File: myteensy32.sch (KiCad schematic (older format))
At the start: 31 parts, among them J1 Conn_01x14_Male, J2 Conn_01x14_Male, J3 USB_C_Receptacle_USB2.0, SW1 RESET, SW2 PROG, U1 MKL04Z32VLC4, U2 MK20DX256VLH7, U3 MCP2562-E-SN, U4 NJM2884U1, Y2 16MHz

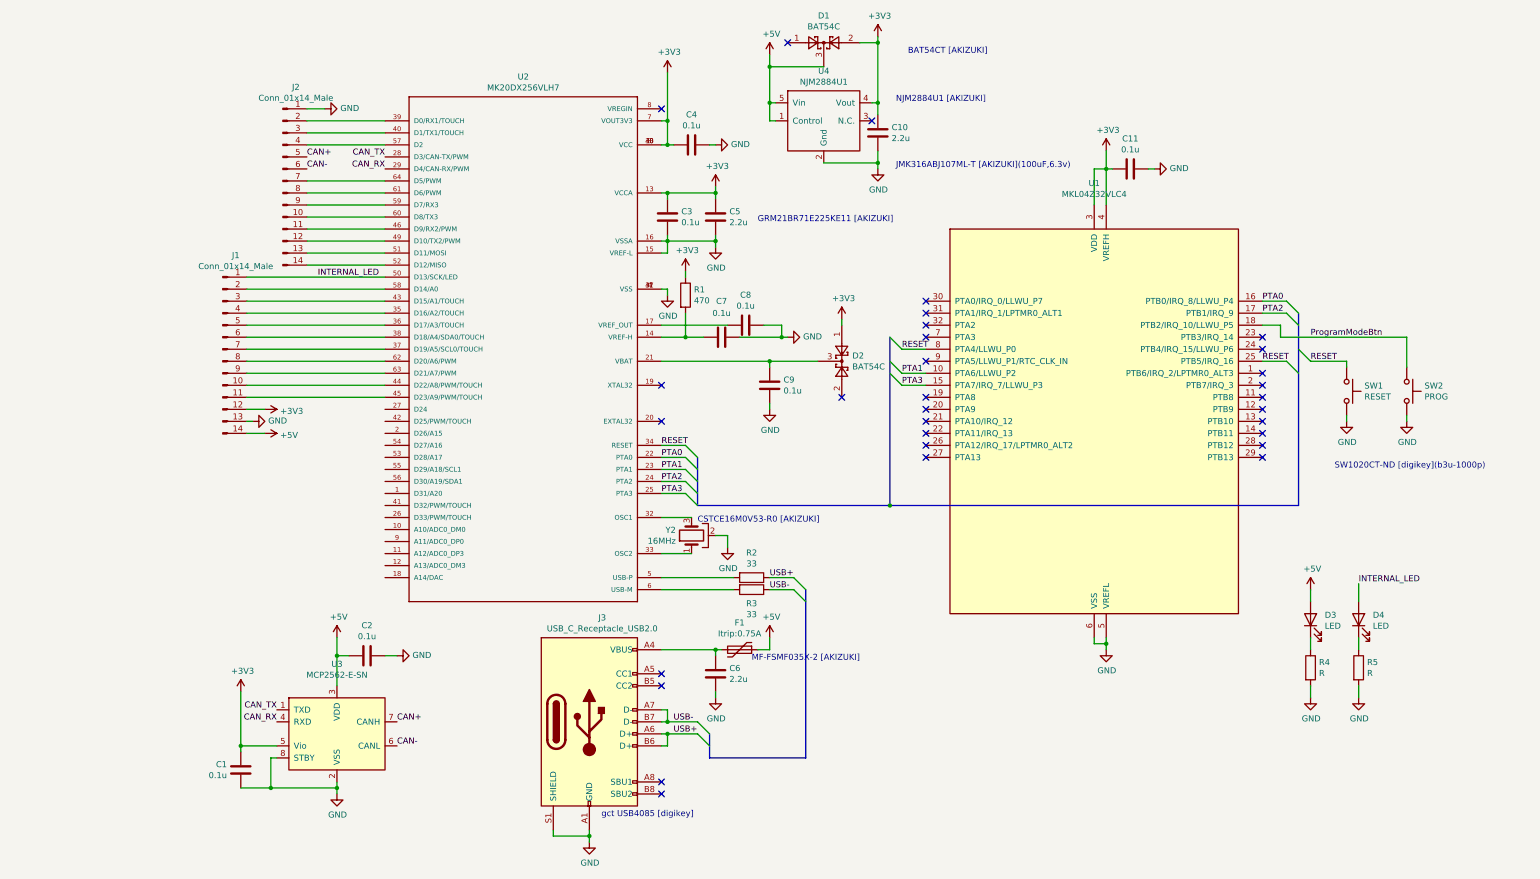
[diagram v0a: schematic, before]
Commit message: Connectorを追加
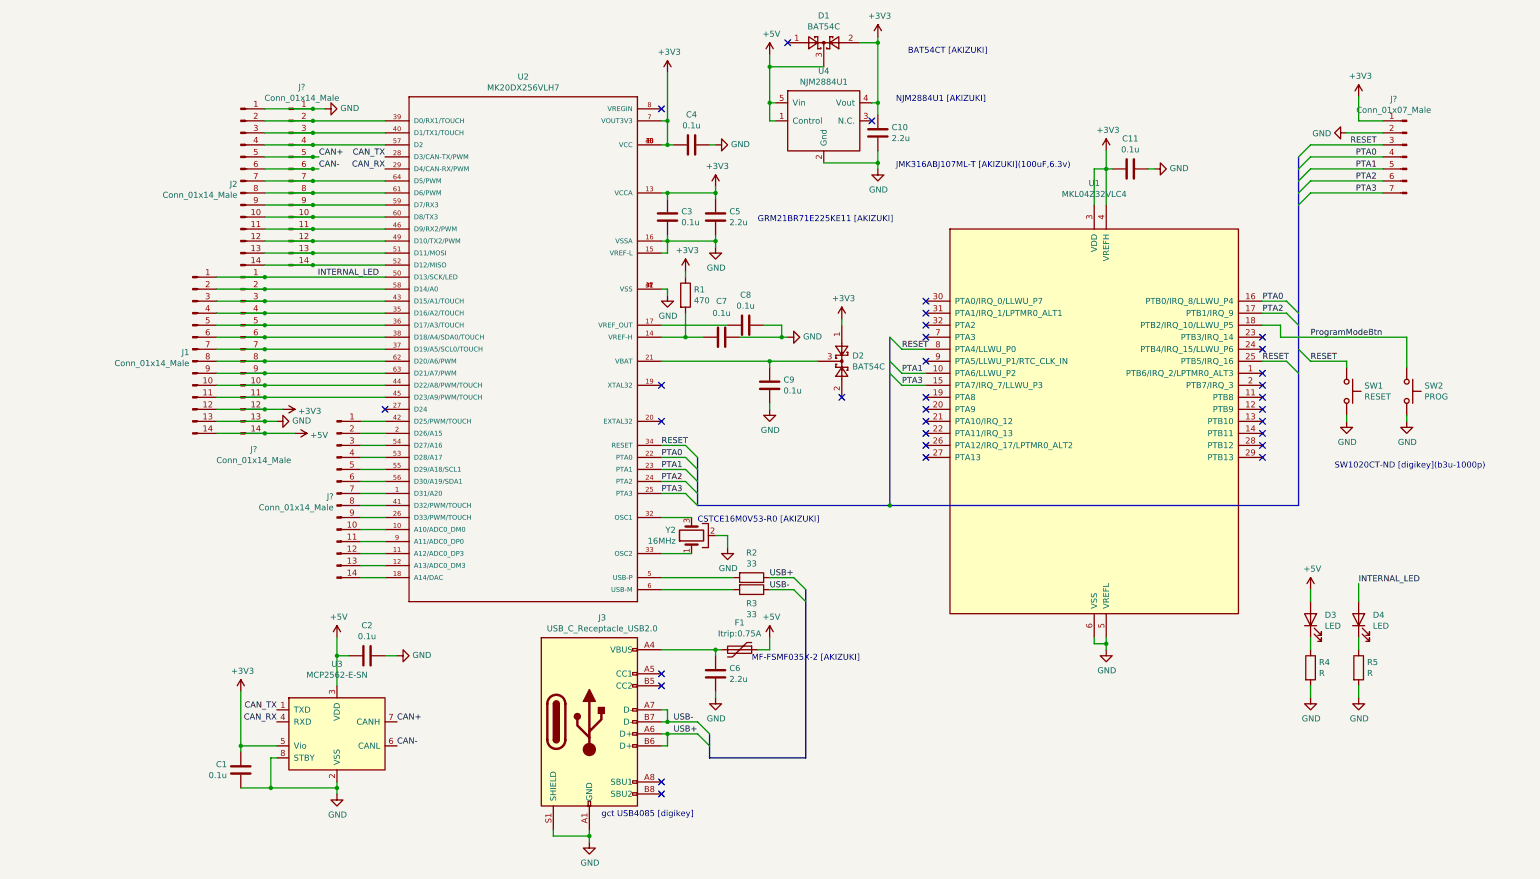
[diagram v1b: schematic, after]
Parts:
- added J?: Conn_01x07_Male, symbol Connector:Conn_01x07_Male
- added J? (x3): Conn_01x14_Male, Connector_PinHeader_2.54mm:PinHeader_1x14_P2.54mm_Vertical, symbol Connector:Conn_01x14_Male
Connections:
- net +3V3: now also J?.1 (Pin_1), J?.12 (Pin_12)
- net +5V: now also J?.14 (Pin_14)
- net CAN+: now also J?.5 (Pin_5)
- net CAN-: now also J?.6 (Pin_6)
- net GND: now also J?.1 (Pin_1), J?.13 (Pin_13), J?.2 (Pin_2)
- net INTERNAL_LED: now also J?.1 (Pin_1)
- net PTA0: now also J?.4 (Pin_4)
- net PTA1: now also J?.5 (Pin_5)
- net PTA2: now also J?.6 (Pin_6)
- net PTA3: now also J?.7 (Pin_7)
- net RESET: now also J?.3 (Pin_3)
- net at U2.1 (D31/A20): now also J?.7 (Pin_7)
- net at U2.10 (A10/ADC0_DM0): now also J?.10 (Pin_10)
- net at U2.11 (A12/ADC0_DP3): now also J?.12 (Pin_12)
- net at U2.12 (A13/ADC0_DM3): now also J?.13 (Pin_13)
- net at U2.18 (A14/DAC): now also J?.14 (Pin_14)
- net at U2.2 (D26/A15): now also J?.2 (Pin_2)
- net at U2.26 (D33/PWM/TOUCH): now also J?.9 (Pin_9)
- net at J1.4 (Pin_4), U2.35 (D16/A2/TOUCH): now also J?.4 (Pin_4)
- net at J1.5 (Pin_5), U2.36 (D17/A3/TOUCH): now also J?.5 (Pin_5)
- net at J1.7 (Pin_7), U2.37 (D19/A5/SCL0/TOUCH): now also J?.7 (Pin_7)
- net at J1.6 (Pin_6), U2.38 (D18/A4/SDA0/TOUCH): now also J?.6 (Pin_6)
- net at J2.2 (Pin_2), U2.39 (D0/RX1/TOUCH): now also J?.2 (Pin_2)
- net at J2.3 (Pin_3), U2.40 (D1/TX1/TOUCH): now also J?.3 (Pin_3)
- net at U2.41 (D32/PWM/TOUCH): now also J?.8 (Pin_8)
- net at U2.42 (D25/PWM/TOUCH): now also J?.1 (Pin_1)
- net at J1.3 (Pin_3), U2.43 (D15/A1/TOUCH): now also J?.3 (Pin_3)
- net at J1.10 (Pin_10), U2.44 (D22/A8/PWM/TOUCH): now also J?.10 (Pin_10)
- net at J1.11 (Pin_11), U2.45 (D23/A9/PWM/TOUCH): now also J?.11 (Pin_11)
- net at J2.11 (Pin_11), U2.46 (D9/RX2/PWM): now also J?.11 (Pin_11)
- net at J2.12 (Pin_12), U2.49 (D10/TX2/PWM): now also J?.12 (Pin_12)
- net at J2.13 (Pin_13), U2.51 (D11/MOSI): now also J?.13 (Pin_13)
- net at J2.14 (Pin_14), U2.52 (D12/MISO): now also J?.14 (Pin_14)
- net at U2.53 (D28/A17): now also J?.4 (Pin_4)
- net at U2.54 (D27/A16): now also J?.3 (Pin_3)
- net at U2.55 (D29/A18/SCL1): now also J?.5 (Pin_5)
- net at U2.56 (D30/A19/SDA1): now also J?.6 (Pin_6)
- net at J2.4 (Pin_4), U2.57 (D2): now also J?.4 (Pin_4)
- net at J1.2 (Pin_2), U2.58 (D14/A0): now also J?.2 (Pin_2)
- net at J2.9 (Pin_9), U2.59 (D7/RX3): now also J?.9 (Pin_9)
- net at J2.10 (Pin_10), U2.60 (D8/TX3): now also J?.10 (Pin_10)
- net at J2.8 (Pin_8), U2.61 (D6/PWM): now also J?.8 (Pin_8)
- net at J1.8 (Pin_8), U2.62 (D20/A6/PWM): now also J?.8 (Pin_8)
- net at J1.9 (Pin_9), U2.63 (D21/A7/PWM): now also J?.9 (Pin_9)
- net at J2.7 (Pin_7), U2.64 (D5/PWM): now also J?.7 (Pin_7)
- net at U2.9 (A11/ADC0_DP0): now also J?.11 (Pin_11)
- no-connect marks 31 -> 32
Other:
- moved on the sheet: J1, J2

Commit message: wideな感じで配線してみる
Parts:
- added H1, H2, H3, H4: MountingHole, mylib:Hole_3.2mm_NPTH, symbol Mechanical:MountingHole
- added J?: Conn_01x21_Male, symbol Connector:Conn_01x21_Male
- J7: renamed from J?; footprint (none) -> Connector_PinSocket_2.54mm:PinSocket_1x07_P2.54mm_Vertical
- gave numbers to parts that had none: 3
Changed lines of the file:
@@
 Connection ~ 6400 1850
 $Comp
-L Connector:Conn_01x07_Male J?
+L Connector:Conn_01x07_Male J7
 U 1 1 5F5015E6
 P 10800 1800
-F 0 "J?" H 10908 2281 50  0000 C CNN
+F 0 "J7" H 10908 2281 50  0000 C CNN
 F 1 "Conn_01x07_Male" H 10908 2190 50  0000 C CNN
-F 2 "" H 10800 1800 50  0001 C CNN
+F 2 "Connector_PinSocket_2.54mm:PinSocket_1x07_P2.54mm_Vertical" H 10800 1800 50  0001 C CNN
 F 3 "~" H 10800 1800 50  0001 C CNN
 	1    10800 1800
@@
 	10600 1700 10000 1700
 $Comp
-L power:GND #PWR?
+L power:GND #PWR0106
 U 1 1 5F5B1720
 P 10300 1600
-F 0 "#PWR?" H 10300 1350 50  0001 C CNN
+F 0 "#PWR0106" H 10300 1350 50  0001 C CNN
 F 1 "GND" V 10305 1472 50  0000 R CNN
 F 2 "" H 10300 1600 50  0001 C CNN
@@
 	10300 1600 10600 1600
 $Comp
-L power:+3V3 #PWR?
+L power:+3V3 #PWR0134
 U 1 1 5F5B9B2F
 P 10400 1300
-F 0 "#PWR?" H 10400 1150 50  0001 C CNN
+F 0 "#PWR0134" H 10400 1150 50  0001 C CNN
 F 1 "+3V3" H 10415 1473 50  0000 C CNN
 F 2 "" H 10400 1300 50  0001 C CNN
@@
 PTA3
 $Comp
-L Connector:Conn_01x14_Male J?
+L Connector:Conn_01x14_Male J4
 U 1 1 5F5C3715
 P 1100 3400
-F 0 "J?" H 1208 2567 50  0000 C CNN
+F 0 "J4" H 1208 2567 50  0000 C CNN
 F 1 "Conn_01x14_Male" H 1208 2476 50  0000 C CNN
 F 2 "Connector_PinHeader_2.54mm:PinHeader_1x14_P2.54mm_Vertical" H 1100 3400 50  0001 C CNN
@@
 	1300 1900 1700 1900
 $Comp
-L Connector:Conn_01x14_Male J?
+L Connector:Conn_01x14_Male J5
 U 1 1 5F64E8EE
 P 1500 2000
-F 0 "J?" H 1608 2781 50  0000 C CNN
+F 0 "J5" H 1608 2781 50  0000 C CNN
 F 1 "Conn_01x14_Male" H 1608 2690 50  0000 C CNN
 F 2 "Connector_PinHeader_2.54mm:PinHeader_1x14_P2.54mm_Vertical" H 1500 2000 50  0001 C CNN
@@
 	1700 2200 1300 2200
 $Comp
-L Connector:Conn_01x14_Male J?
+L Connector:Conn_01x14_Male J6
 U 1 1 5F6768BE
 P 1900 4600
-F 0 "J?" H 1872 4574 50  0000 R CNN
+F 0 "J6" H 1872 4574 50  0000 R CNN
 F 1 "Conn_01x14_Male" H 1872 4483 50  0000 R CNN
 F 2 "Connector_PinHeader_2.54mm:PinHeader_1x14_P2.54mm_Vertical" H 1900 4600 50  0001 C CNN
@@
 	2300 5300 2100 5300
 NoConn ~ 2300 3900
+$Comp
+L Mechanical:MountingHole H1
+U 1 1 5F53C8C0
+P 6250 6750
+F 0 "H1" H 6350 6796 50  0000 L CNN
+F 1 "MountingHole" H 6350 6705 50  0000 L CNN
+F 2 "mylib:Hole_3.2mm_NPTH" H 6250 6750 50  0001 C CNN
+F 3 "~" H 6250 6750 50  0001 C CNN
+	1    6250 6750
+	1    0    0    -1
+$EndComp
+$Comp
+L Mechanical:MountingHole H2
+U 1 1 5F53E0CD
+P 6250 6950
+F 0 "H2" H 6350 6996 50  0000 L CNN
+F 1 "MountingHole" H 6350 6905 50  0000 L CNN
+F 2 "mylib:Hole_3.2mm_NPTH" H 6250 6950 50  0001 C CNN
+F 3 "~" H 6250 6950 50  0001 C CNN
+	1    6250 6950
+	1    0    0    -1
+$EndComp
+$Comp
+L Mechanical:MountingHole H3
+U 1 1 5F53E326
+P 6250 7150
+F 0 "H3" H 6350 7196 50  0000 L CNN
+F 1 "MountingHole" H 6350 7105 50  0000 L CNN
+F 2 "mylib:Hole_3.2mm_NPTH" H 6250 7150 50  0001 C CNN
+F 3 "~" H 6250 7150 50  0001 C CNN
+	1    6250 7150
+	1    0    0    -1
+$EndComp
+$Comp
+L Mechanical:MountingHole H4
+U 1 1 5F53E56E
+P 6250 7350
+F 0 "H4" H 6350 7396 50  0000 L CNN
+F 1 "MountingHole" H 6350 7305 50  0000 L CNN
+F 2 "mylib:Hole_3.2mm_NPTH" H 6250 7350 50  0001 C CNN
+F 3 "~" H 6250 7350 50  0001 C CNN
+	1    6250 7350
+	1    0    0    -1
+$EndComp
+$Comp
+L Connector:Conn_01x21_Male J?
+U 1 1 5F5DBB58
+P -550 2500
+F 0 "J?" H -442 3681 50  0000 C CNN
+F 1 "Conn_01x21_Male" H -442 3590 50  0000 C CNN
+F 2 "" H -550 2500 50  0001 C CNN
+F 3 "~" H -550 2500 50  0001 C CNN
+	1    -550 2500
+	1    0    0    -1
+$EndComp
 Wire Bus Line
 	5000 6600 5000 6800
